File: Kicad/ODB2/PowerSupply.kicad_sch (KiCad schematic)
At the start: 54 parts, among them J2 Batt3v7, J3 Batt12V, Q1 MMBT3904, Q2 IRFR5505TRPBF, Q3 PJA3411_R1_00001, U2 TPS61201DRCR, U3 LM1085-5.0, U8 MCP1727-1802xMF

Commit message: fix 3v7_r2
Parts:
- 3v7_R2: value 27k 1% -> 12k 1%
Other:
- note added: "VOLTAGE DIVIDER RATIO IS 0.8929"
- note removed: "VOLTAGE DIVIDER RATIO IS 0.7874"
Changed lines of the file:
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@@
 		)
 	)
-	(text "VOLTAGE DIVIDER RATIO IS 0.7874"
+	(text "VOLTAGE DIVIDER RATIO IS 0.8929"
 		(exclude_from_sim no)
 		(at 35.56 143.51 0)
@@
 			)
 		)
-		(property "Value" "27k 1%"
+		(property "Value" "12k 1%"
 			(at 38.1 139.7 90)
 			(effects

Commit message: WIP on ODB
buzzer résistance et footprints ampliop et autre
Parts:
- R1V8_R2: footprint (none) -> Resistor_SMD:R_0805_2012Metric
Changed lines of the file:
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@@
 			)
 		)
-		(property "Footprint" ""
+		(property "Footprint" "Resistor_SMD:R_0805_2012Metric"
 			(at 29.718 185.42 90)
 			(effects

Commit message: fix label crystal + capacité découplage fix + add mosfet 6v isolation footprint
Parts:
- Q2: footprint custom_footprints:PG-TO252AA_INF -> Library:PG-TO252AA_INF
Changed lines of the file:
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@@
 			)
 		)
-		(property "Footprint" "custom_footprints:PG-TO252AA_INF"
+		(property "Footprint" "Library:PG-TO252AA_INF"
 			(at 222.25 43.18 0)
 			(effects

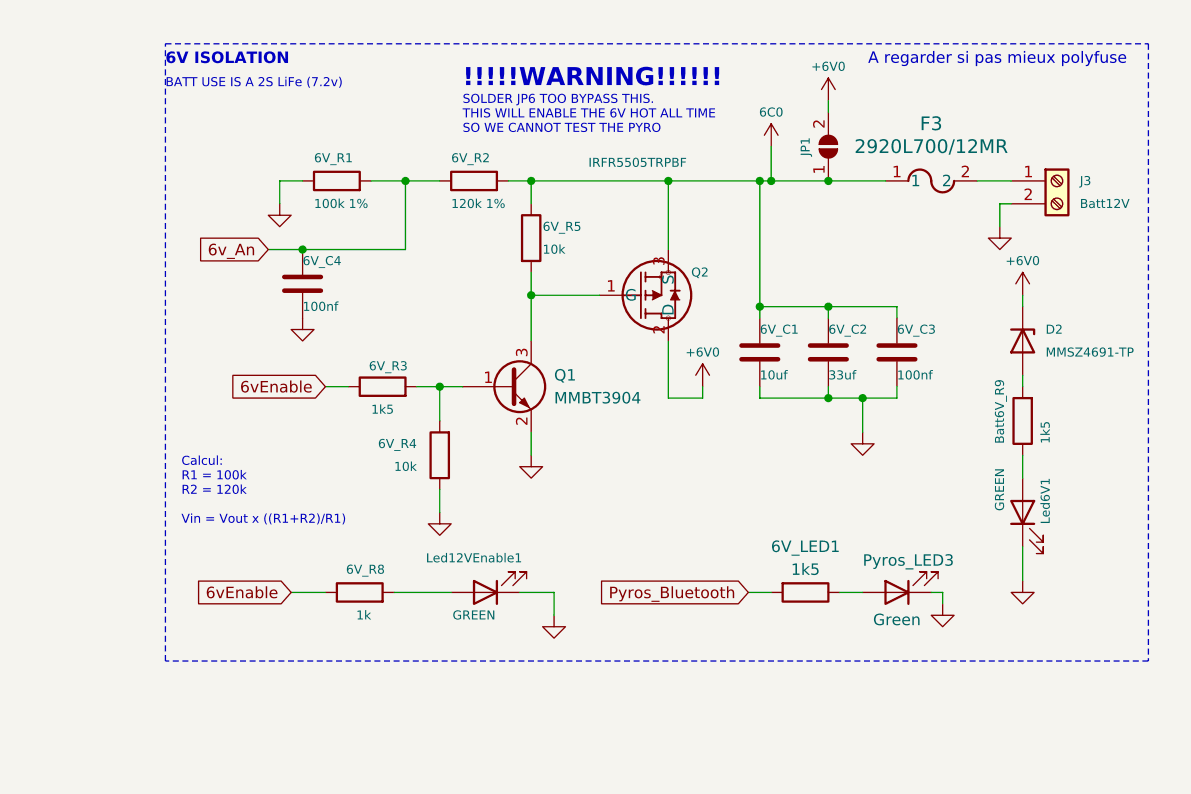
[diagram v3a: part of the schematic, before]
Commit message: Changed label 6v to 6v6 and changed circuit for the 6v6 batt led
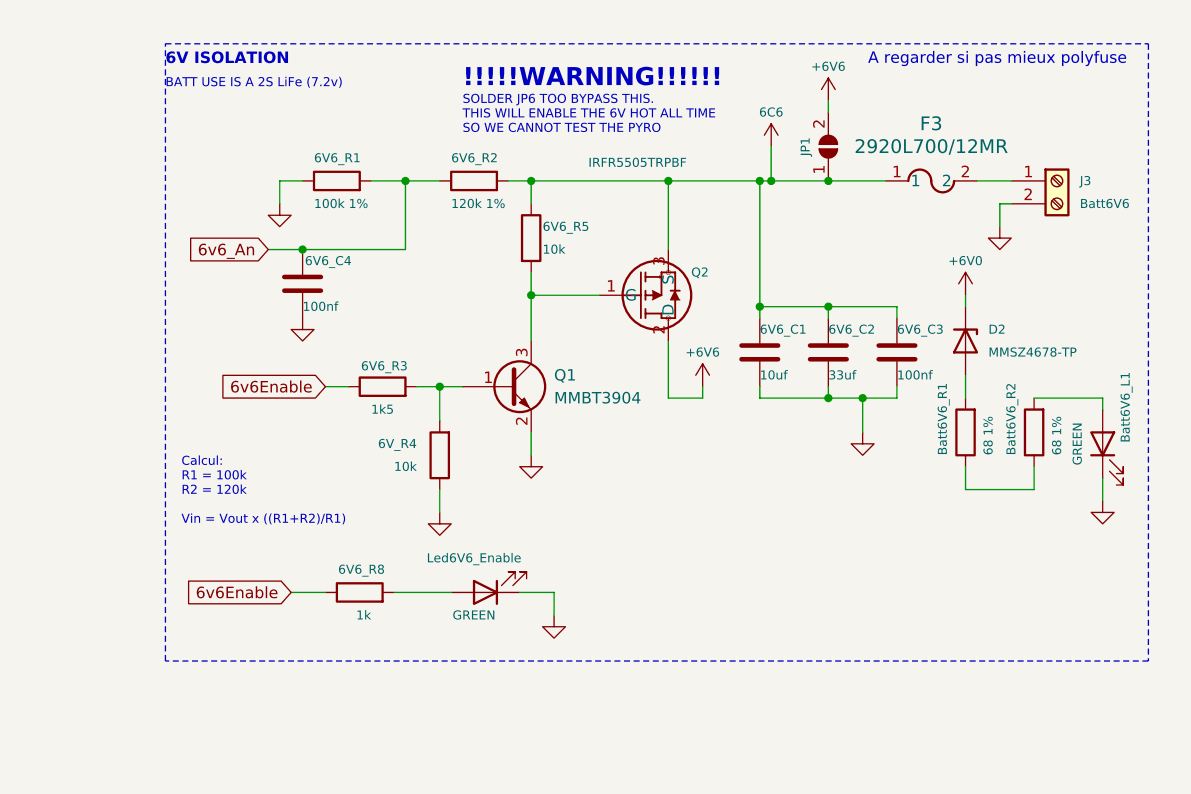
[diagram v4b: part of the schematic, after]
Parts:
- removed 6V_LED1: 1k5, Resistor_SMD:R_0805_2012Metric, symbol Device:R
- removed Pyros_LED3: Green, LED_SMD:LED_0805_2012Metric, symbol Device:LED
- added Batt6V6_R2: 68 1%, Resistor_SMD:R_0805_2012Metric, symbol Device:R
- Batt6V6_R1: renamed from Batt6V_R9; value 1k5 -> 68 1%
- D2: value MMSZ4691-TP -> MMSZ4678-TP
- J3: value Batt12V -> Batt6V6
- renumbered 6V_C1 to 6V6_C1, 6V_C2 to 6V6_C2, 6V_C3 to 6V6_C3, 6V_C4 to 6V6_C4, 6V_R1 to 6V6_R1, 6V_R2 to 6V6_R2, 6V_R3 to 6V6_R3, 6V_R5 to 6V6_R5, 6V_R8 to 6V6_R8, Led6V1 to Batt6V6_L1, Led12VEnable1 to Led6V6_Enable
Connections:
- net +6V0: no longer JP1.2 (B), Q2.2 (D)
- net at Batt6V6_R1.1: now also Batt6V6_R2.1; no longer Batt6V6_L1.2 (A)
- net 6C0 renamed 6C6
- net 6vEnable renamed 6v6Enable
- net 6v_An renamed 6v6_An
- new net: Batt6V6_L1.2 (A), Batt6V6_R2.2
- new net +6V6: JP1.2 (B), Q2.2 (D)
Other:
- moved on the sheet: Batt6V6_L1, Batt6V6_R1, D2

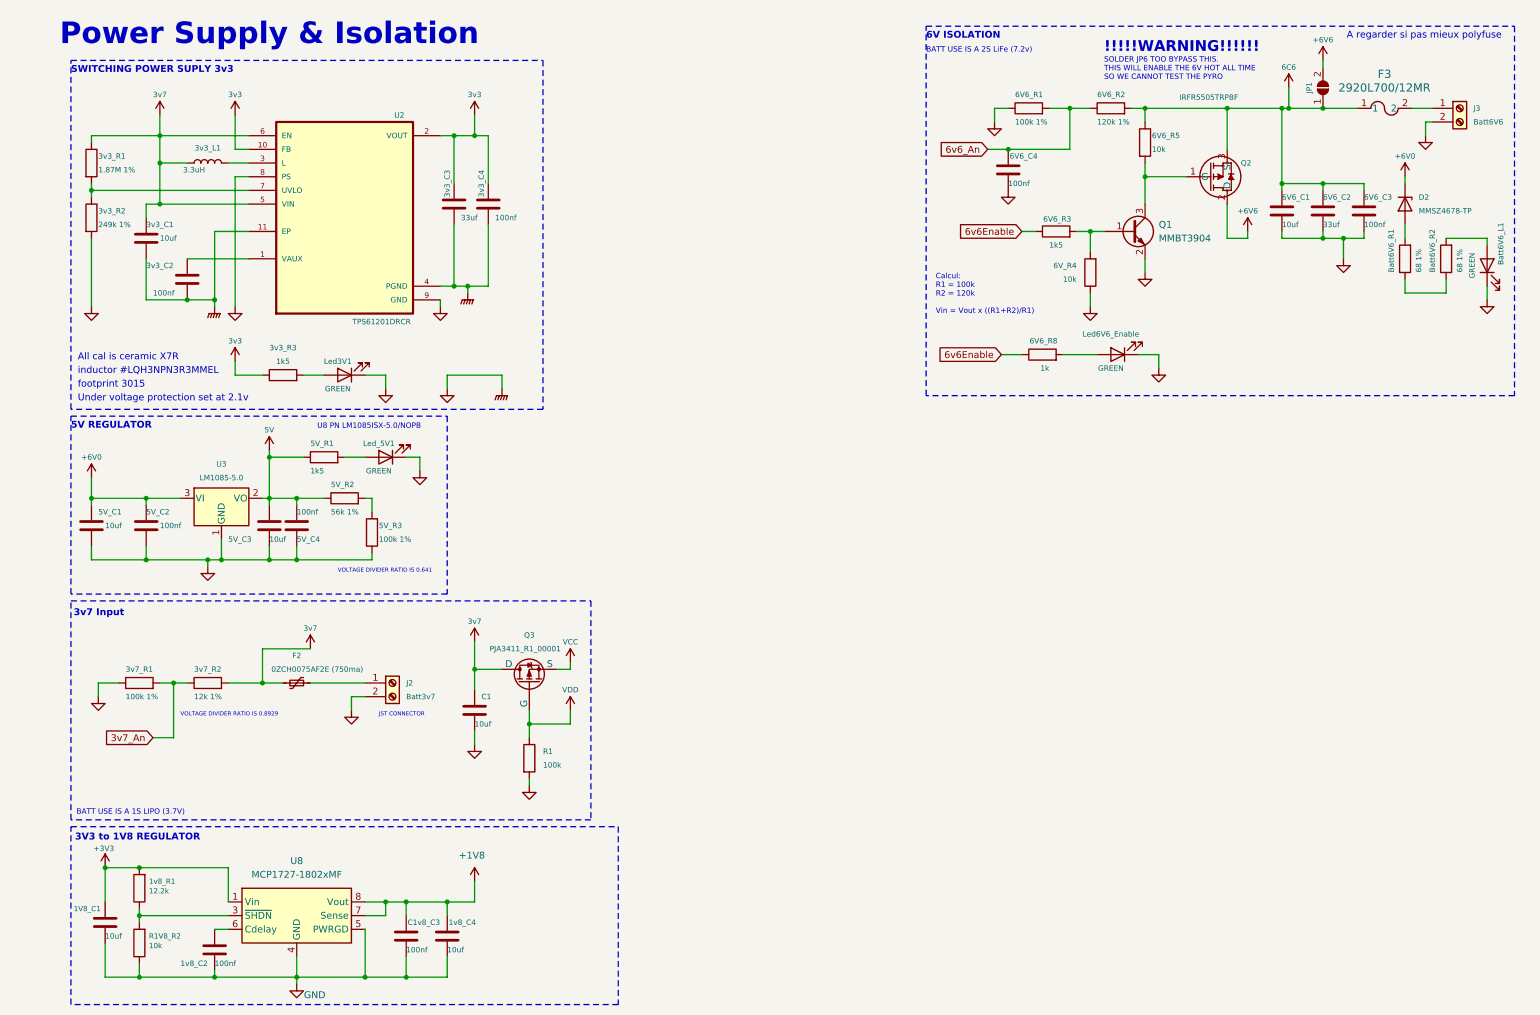
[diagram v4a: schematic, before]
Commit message: changer LiFePO4 pour LiPo
recalculer le bon ration pour l'ADC du 4v2 input (anciennement 3v7 input) et modifier ces labels associées

modifier le bon ration (je crois) pour l'ADC du 7v4 isolation (anciennement 6v isolation) et modifier ces labels associées
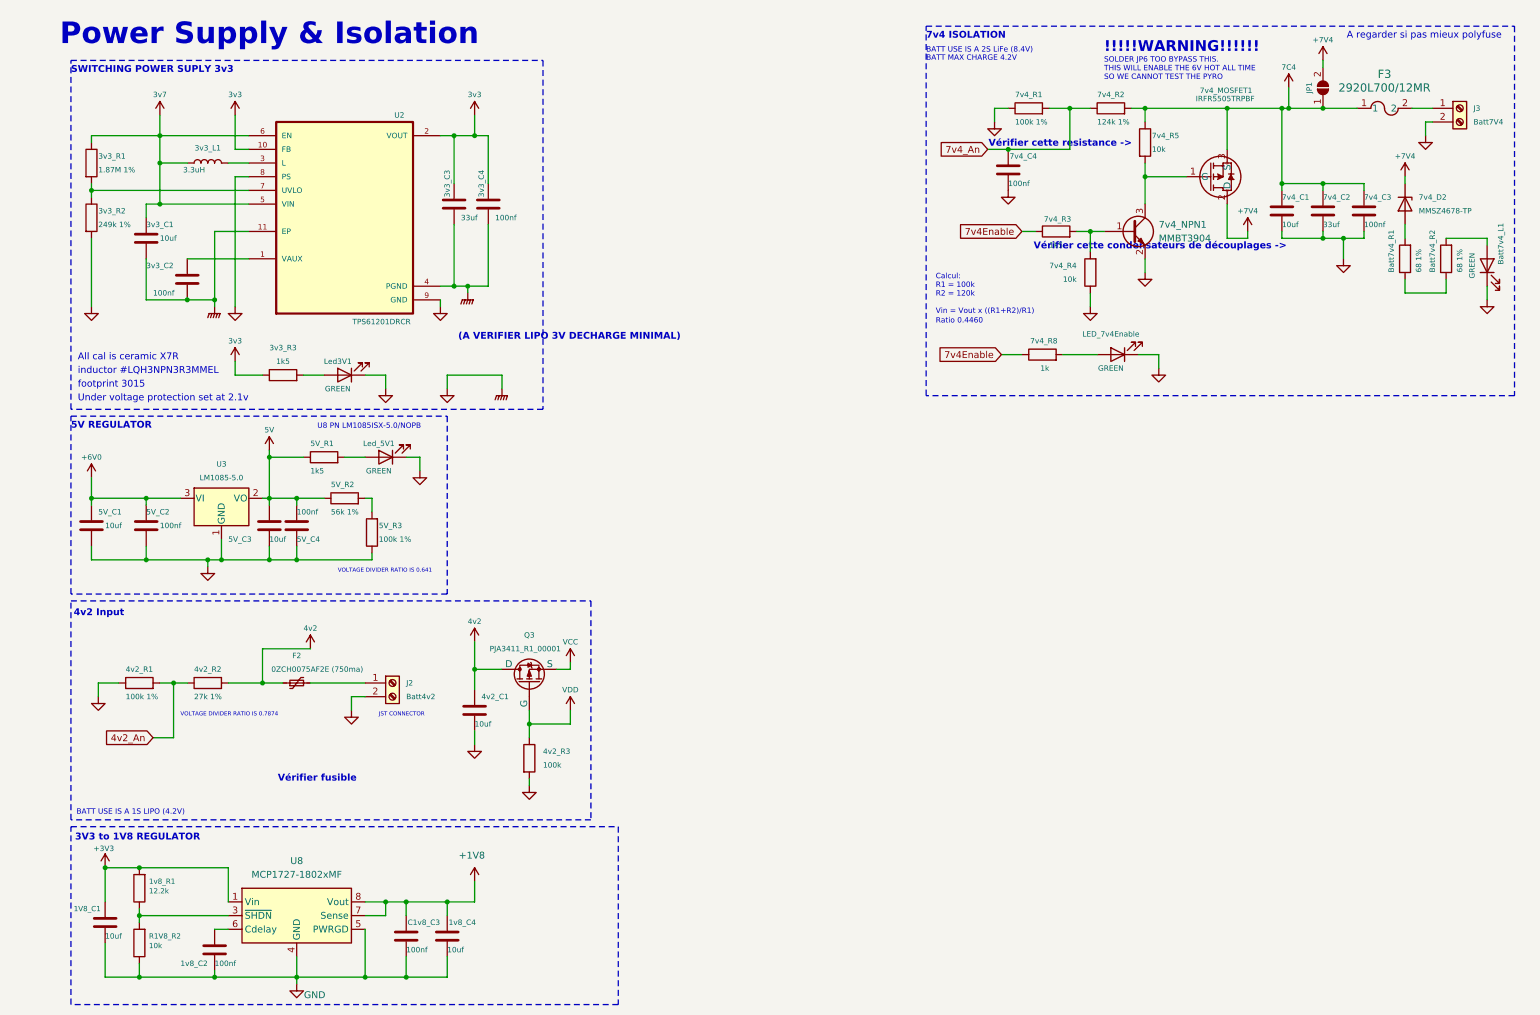
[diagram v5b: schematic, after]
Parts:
- 4v2_R2: renamed from 3v7_R2; value 12k 1% -> 27k 1%
- 7v4_R2: renamed from 6V6_R2; value 120k 1% -> 124k 1%
- J2: value Batt3v7 -> Batt4v2
- J3: value Batt6V6 -> Batt7V4
- renumbered C1 to 4v2_C1, 3v7_R1 to 4v2_R1, R1 to 4v2_R3, 6V6_C1 to 7v4_C1, 6V6_C2 to 7v4_C2, 6V6_C3 to 7v4_C3, 6V6_C4 to 7v4_C4, D2 to 7v4_D2, Q2 to 7v4_MOSFET1, Q1 to 7v4_NPN1, 6V6_R1 to 7v4_R1, 6V6_R3 to 7v4_R3, 6V_R4 to 7v4_R4, 6V6_R5 to 7v4_R5, 6V6_R8 to 7v4_R8, Batt6V6_L1 to Batt7v4_L1, Batt6V6_R1 to Batt7v4_R1, Batt6V6_R2 to Batt7v4_R2, Led6V6_Enable to LED_7v4Enable
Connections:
- net +6V0: no longer 7v4_D2.1 (K)
- net 3v7: no longer 4v2_C1.1, 4v2_R2.2, F2.1, Q3.3 (D)
- net +6V6 renamed +7V4
- net +7V4: now also 7v4_D2.1 (K)
- net 3v7_An renamed 4v2_An
- net 6C6 renamed 7C4
- net 6v6Enable renamed 7v4Enable
- net 6v6_An renamed 7v4_An
- new net 4v2: 4v2_C1.1, 4v2_R2.2, F2.1, Q3.3 (D)
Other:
- note added: "(A VERIFIER LIPO 3V DECHARGE MINIMAL)"
- note added: "4v2 Input"
- note added: "7v4 ISOLATION"
- note added: "BATT MAX CHARGE 4.2V"
- note added: "BATT USE IS A 1S LIPO (4.2V)"
- note added: "BATT USE IS A 2S LiFe (8.4V)"
- note added: "Ratio 0.4460"
- note added: "VOLTAGE DIVIDER RATIO IS 0.7874"
- note added: "Vérifier cette condensateurs de découplages ->"
- note added: "Vérifier cette resistance ->"
- note added: "Vérifier fusible"
- note removed: "3v7 Input"
- note removed: "6V ISOLATION"
- note removed: "BATT USE IS A 1S LIPO (3.7V)"
- note removed: "BATT USE IS A 2S LiFe (7.2v)"
- note removed: "VOLTAGE DIVIDER RATIO IS 0.8929"

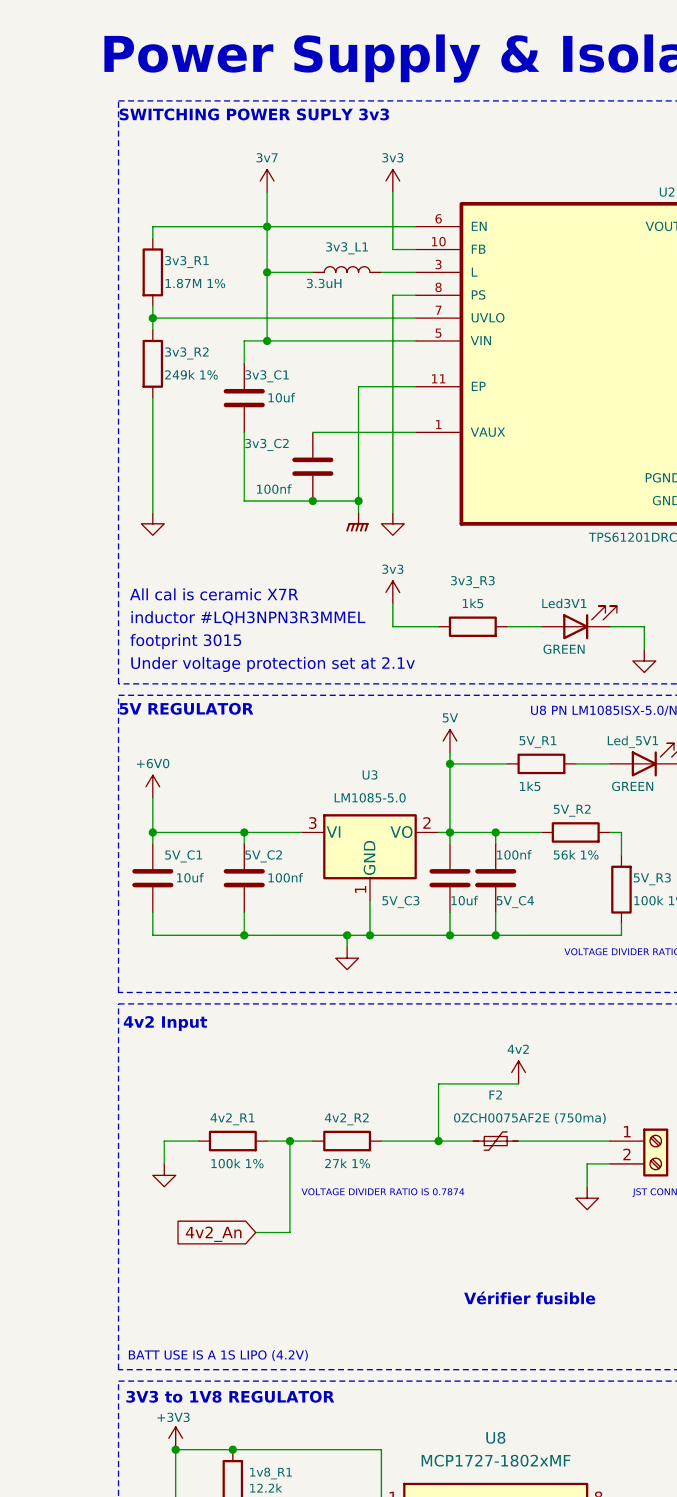
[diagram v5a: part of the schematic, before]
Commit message: fixed r value
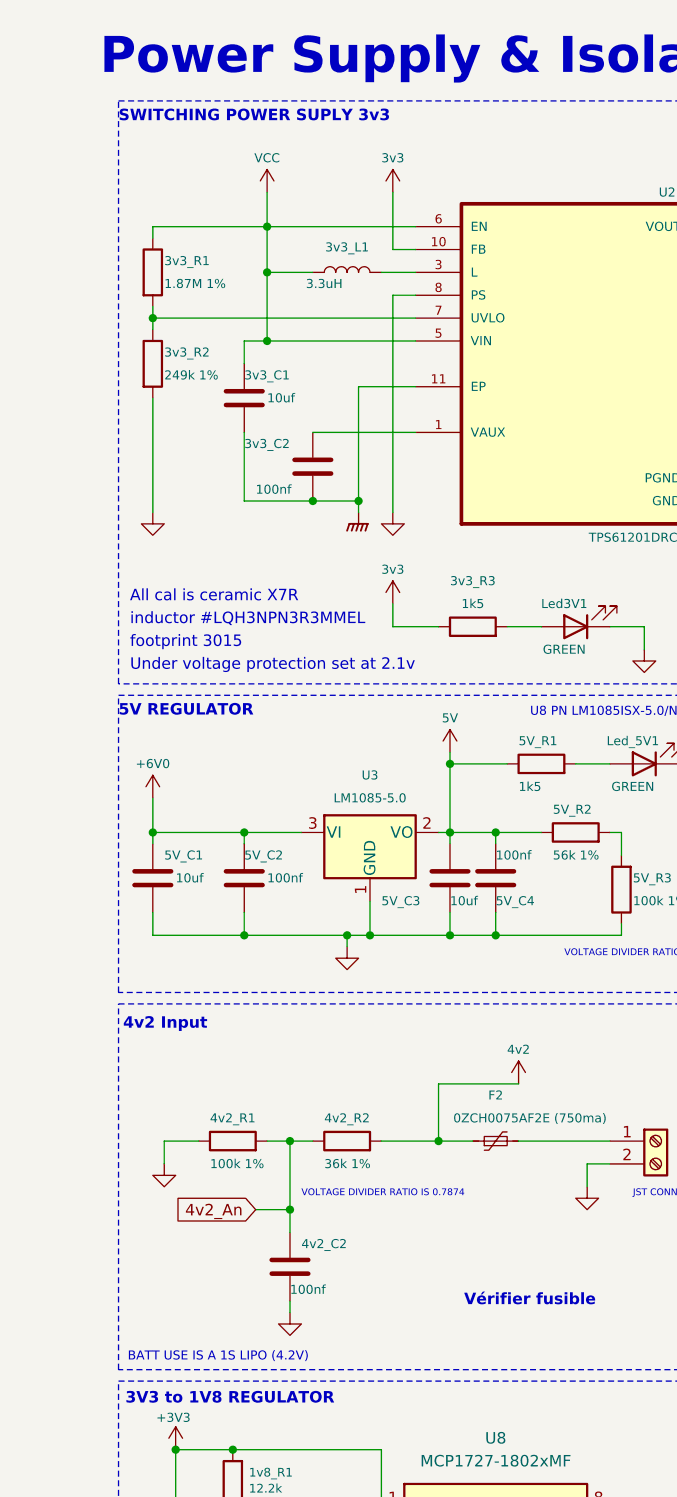
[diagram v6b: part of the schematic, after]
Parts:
- added 4v2_C2: 100nf, Capacitor_SMD:C_0805_2012Metric, symbol Device:C
- 4v2_R2: value 27k 1% -> 36k 1%
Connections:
- net 3v7 is gone; now on net VCC: 3v3_C1.1, 3v3_L1.1, 3v3_R1.1, U2.5 (VIN), U2.6 (EN)
- net 4v2_An: now also 4v2_C2.1
- net GND: now also 4v2_C2.2
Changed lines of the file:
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@@
 	)
 	(junction
+		(at 34.29 144.78)
+		(diameter 0)
+		(color 0 0 0 0)
+	)
+	(junction
 		(at 241.3 30.48)
 		(diameter 0)
@@
 	(wire
 		(pts
+			(xy 34.29 154.94) (xy 34.29 156.21)
+		)
+		(stroke
+			(width 0)
+			(type default)
+		)
+	)
+	(wire
+		(pts
 			(xy 92.71 52.07) (xy 92.71 63.5)
 		)
@@
 	(wire
 		(pts
-			(xy 30.48 147.32) (xy 34.29 147.32)
-		)
-		(stroke
-			(width 0)
-			(type default)
-		)
-	)
-	(wire
-		(pts
 			(xy 27.94 171.45) (xy 44.45 171.45)
 		)
@@
 	(wire
 		(pts
+			(xy 34.29 144.78) (xy 34.29 137.16)
+		)
+		(stroke
+			(width 0)
+			(type default)
+		)
+	)
+	(wire
+		(pts
 			(xy 86.36 35.56) (xy 86.36 44.45)
 		)
@@
 	(wire
 		(pts
-			(xy 34.29 147.32) (xy 34.29 137.16)
+			(xy 34.29 147.32) (xy 34.29 144.78)
 		)
 		(stroke
@@
 	(wire
 		(pts
+			(xy 30.48 144.78) (xy 34.29 144.78)
+		)
+		(stroke
+			(width 0)
+			(type default)
+		)
+	)
+	(wire
+		(pts
 			(xy 77.47 187.96) (xy 77.47 191.77)
 		)
@@
 	(global_label "4v2_An"
 		(shape input)
-		(at 30.48 147.32 180)
+		(at 30.48 144.78 180)
 		(fields_autoplaced yes)
 		(effects
@@
 		)
 		(property "Intersheetrefs" "${INTERSHEET_REFS}"
-			(at 20.903 147.32 0)
+			(at 20.903 144.78 0)
 			(effects
 				(font
@@
 	(symbol
 		(lib_id "Device:C")
+		(at 34.29 151.13 0)
+		(unit 1)
+		(exclude_from_sim no)
+		(in_bom yes)
+		(on_board yes)
+		(dnp no)
+		(property "Reference" "4v2_C2"
+			(at 35.56 148.59 0)
+			(effects
+				(font
+					(size 1 1)
+				)
+				(justify left)
+			)
+		)
+		(property "Value" "100nf"
+			(at 34.29 153.67 0)
+			(effects
+				(font
+					(size 1 1)
+				)
+				(justify left)
+			)
+		)
+		(property "Footprint" "Capacitor_SMD:C_0805_2012Metric"
+			(at 35.2552 154.94 0)
+			(effects
+				(font
+					(size 1 1)
+				)
+				(hide yes)
+			)
+		)
+		(property "Datasheet" "~"
+			(at 34.29 151.13 0)
+			(effects
+				(font
+					(size 1 1)
+				)
+				(hide yes)
+			)
+		)
+		(property "Description" ""
+			(at 34.29 151.13 0)
+			(effects
+				(font
+					(size 1.27 1.27)
+				)
+				(hide yes)
+			)
+		)
+		(pin "1"
+		)
+		(pin "2"
+		)
+		(instances
+			(project "ODB2"
+				(path "/4b06c5d1-aa8b-48ed-8972-b43a60cfab78/a0dfa29e-ccca-4096-8481-c7e33c67aac5"
+					(reference "4v2_C2")
+					(unit 1)
+				)
+			)
+		)
+	)
+	(symbol
+		(lib_id "Device:C")
 		(at 240.03 49.53 0)
 		(unit 1)
@@
 	)
 	(symbol
+		(lib_id "power:GND")
+		(at 34.29 156.21 0)
+		(unit 1)
+		(exclude_from_sim no)
+		(in_bom yes)
+		(on_board yes)
+		(dnp no)
+		(fields_autoplaced yes)
+		(property "Reference" "#PWR077"
+			(at 34.29 162.56 0)
+			(effects
+				(font
+					(size 1 1)
+				)
+				(hide yes)
+			)
+		)
+		(property "Value" "GND"
+			(at 34.29 161.29 0)
+			(effects
+				(font
+					(size 1 1)
+				)
+				(hide yes)
+			)
+		)
+		(property "Footprint" ""
+			(at 34.29 156.21 0)
+			(effects
+				(font
+					(size 1 1)
+				)
+				(hide yes)
+			)
+		)
+		(property "Datasheet" ""
+			(at 34.29 156.21 0)
+			(effects
+				(font
+					(size 1 1)
+				)
+				(hide yes)
+			)
+		)
+		(property "Description" ""
+			(at 34.29 156.21 0)
+			(effects
+				(font
+					(size 1.27 1.27)
+				)
+				(hide yes)
+			)
+		)
+		(pin "1"
+		)
+		(instances
+			(project "ODB2"
+				(path "/4b06c5d1-aa8b-48ed-8972-b43a60cfab78/a0dfa29e-ccca-4096-8481-c7e33c67aac5"
+					(reference "#PWR077")
+					(unit 1)
+				)
+			)
+		)
+	)
+	(symbol
 		(lib_id "Device:C")
 		(at 36.83 62.23 0)
@@
 			)
 		)
-		(property "Value" "27k 1%"
+		(property "Value" "36k 1%"
 			(at 38.1 139.7 90)
 			(effects
@@
 			)
 		)
-		(property "Value" "3v7"
+		(property "Value" "VCC"
 			(at 31.75 27.94 0)
 			(effects
